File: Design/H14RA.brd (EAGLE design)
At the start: 34.6 x 30 mm, 42 parts, among them P2 HEXABIT_17.32, Q1 MMBT3904LT1, Q2 MMBT3904LT1, Q3 MMBT3904LT1, Q4 MMBT3904LT1, Q5 MMBT3904LT1, Q6 MMBT3904LT1, U1 STM32G0B1CEU6N, U2 LM2775-Q1, X1 XTALL_CSTCE8M00G52

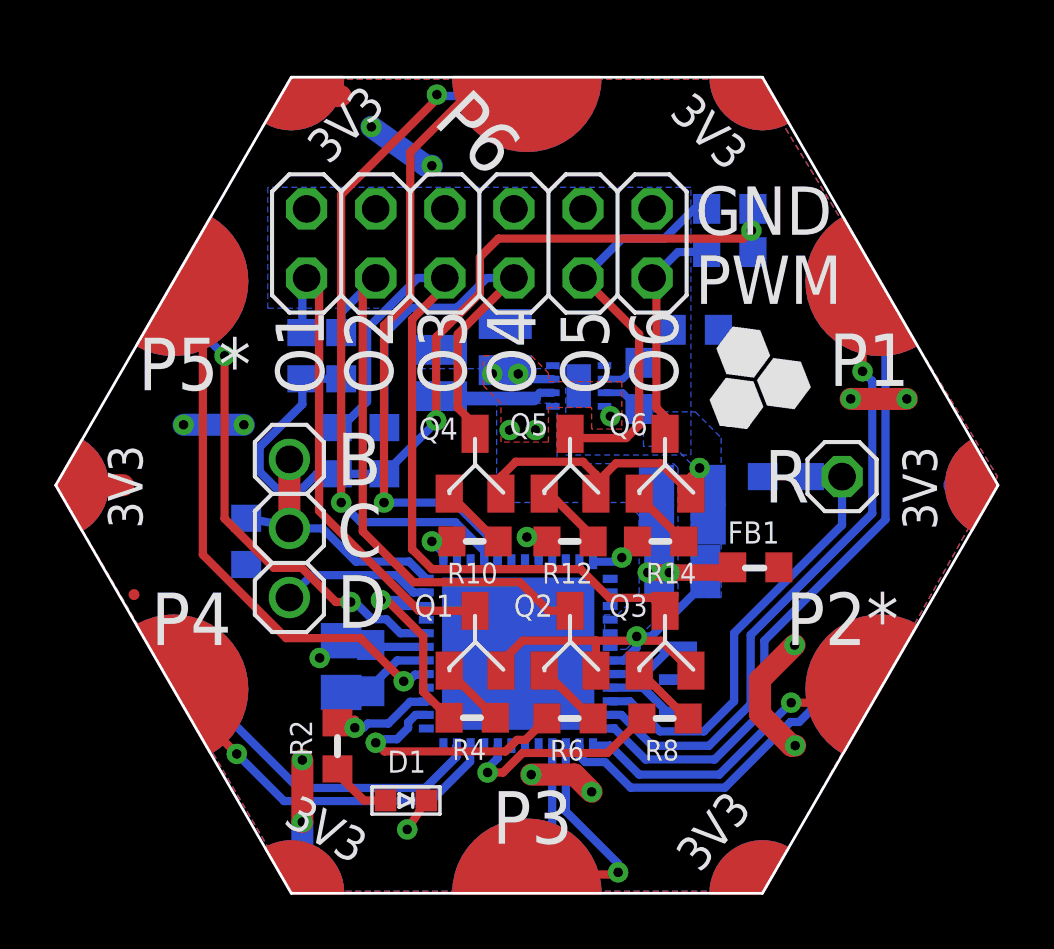
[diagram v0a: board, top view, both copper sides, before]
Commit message: -Fix the issue with an MCU pin that cannot output PWM signals. -Update the design and BOM to reflect the latest modifications in the Platform Hardware rules.
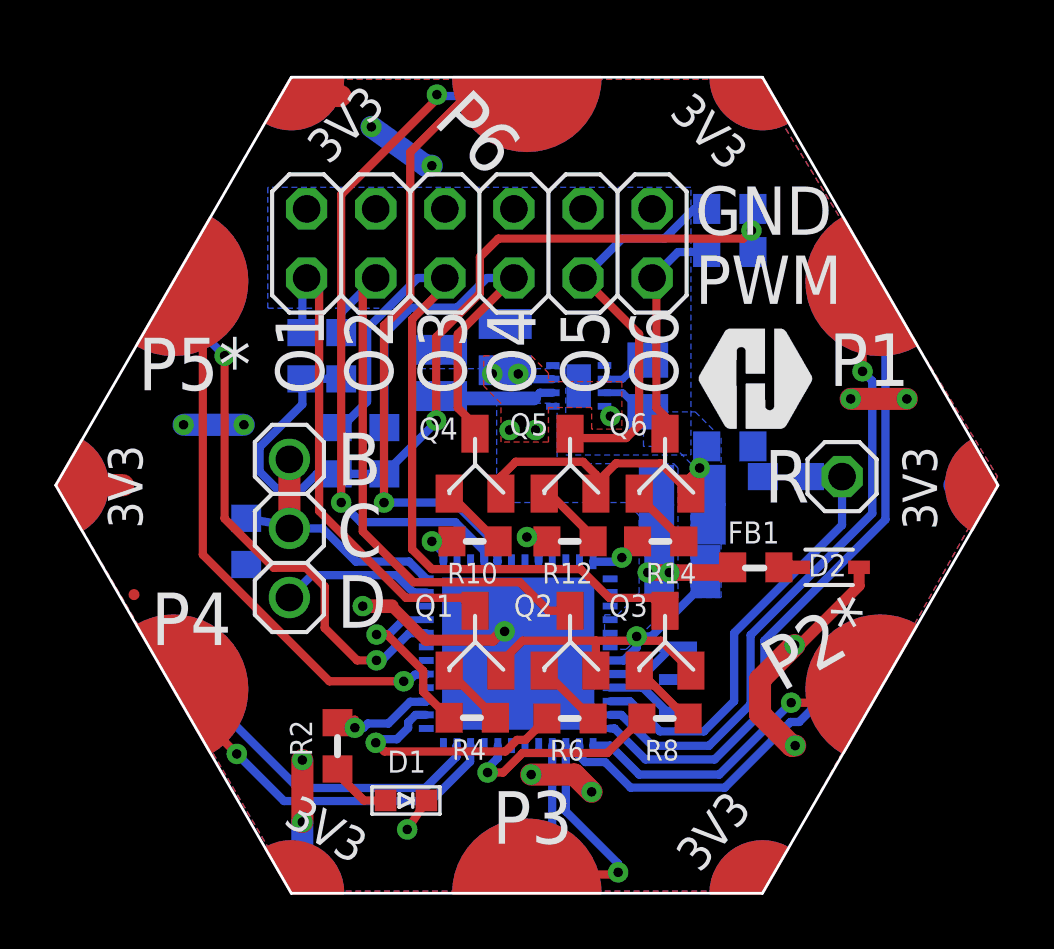
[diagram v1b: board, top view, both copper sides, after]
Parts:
- removed C6: 100nF, HEXABITZ_RCLS:C-0603
- removed C7: 4.7uF, HEXABITZ_RCLS:C-0805-POL
- added D2: BOURNS_CDSOD323-T03SCBOURNS_CDSOD323-T03SC_0_0, HEXABITZ_RCLS:BOURNS_CDSOD323-T03SC_0
- added TRIMBLE-LOGO2: HEXA-LOGO, HEXABITZ_USER_INTERFACE_PARTS:HEXA-LOGO
- C14: device HEXABITZ_RCLS:C-0603 -> HEXABITZ_RCLS:C-0805
- U1: value STM32G0B1CEU6N -> STM32G0B1CEU6QFN_B1CEU6_STM-L; device HEXABITZ_ICs:HEXABITZ_ICS_QFN_B1CEU6_STM-L -> HEXABITZ_ICs:QFN_B1CEU6_STM-L
- moved R1 4.47 mm to (7.46, 16.5)
- moved C14 0.32 mm to (4.45, 18.7)
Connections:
- net C1: now also U1.33; no longer U1.34
- net GND: now also D2.1; no longer C6.2, C7.2, U1.24, U1.25, U1.30
- net VDD: now also D2.2; no longer C6.1, C7.1, U1.31
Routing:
- net GND: track 19.9 -> 28.3 mm, vias 9 -> 11
- net VDD: track 13.8 -> 10.3 mm, vias 5 -> 4
- net USART1_RX: track 18.1 -> 19.8 mm
- net C1: track 7.26 -> 6.44 mm
